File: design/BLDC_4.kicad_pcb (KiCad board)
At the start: 2 copper layers, 80 x 48.9 mm, 99 parts, among them J1 Conn_01x04, P1 PWR_COMM, P2 IN+, P3 IN-, P4 MOTOR3, P5 MOTOR2, P6 MOTOR1, P7 SWD, Q1 Si2302CDS, Q2 Si2302CDS, Q3 Si2302CDS, Q4 Si2302CDS, Q5 Si2302CDS, Q6 Si2302CDS, U1 DRV8302, U2 TC2117, U3 STM32F40X_LQFP64, X1 8MHz 10ppm

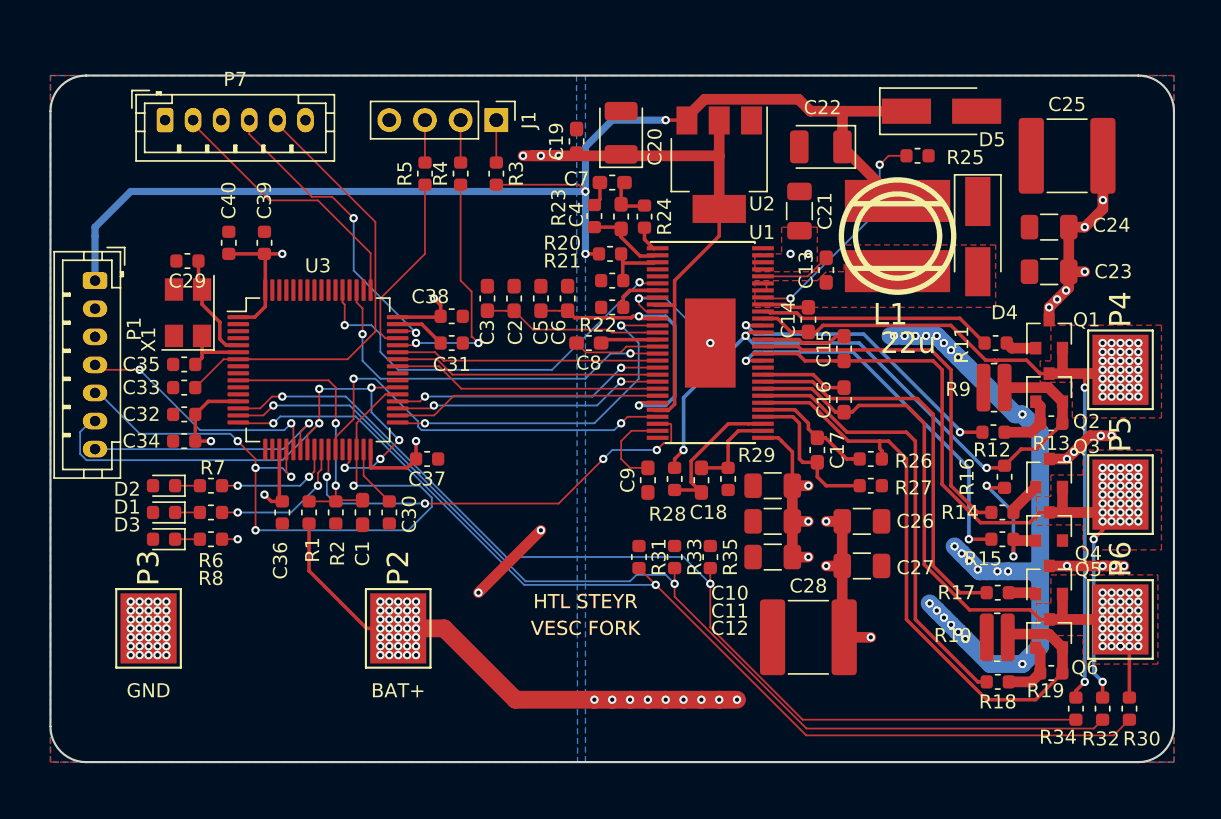
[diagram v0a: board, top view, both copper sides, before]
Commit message: Strengthening fills for output stage. Adding GND Fill
More to come :godmode:
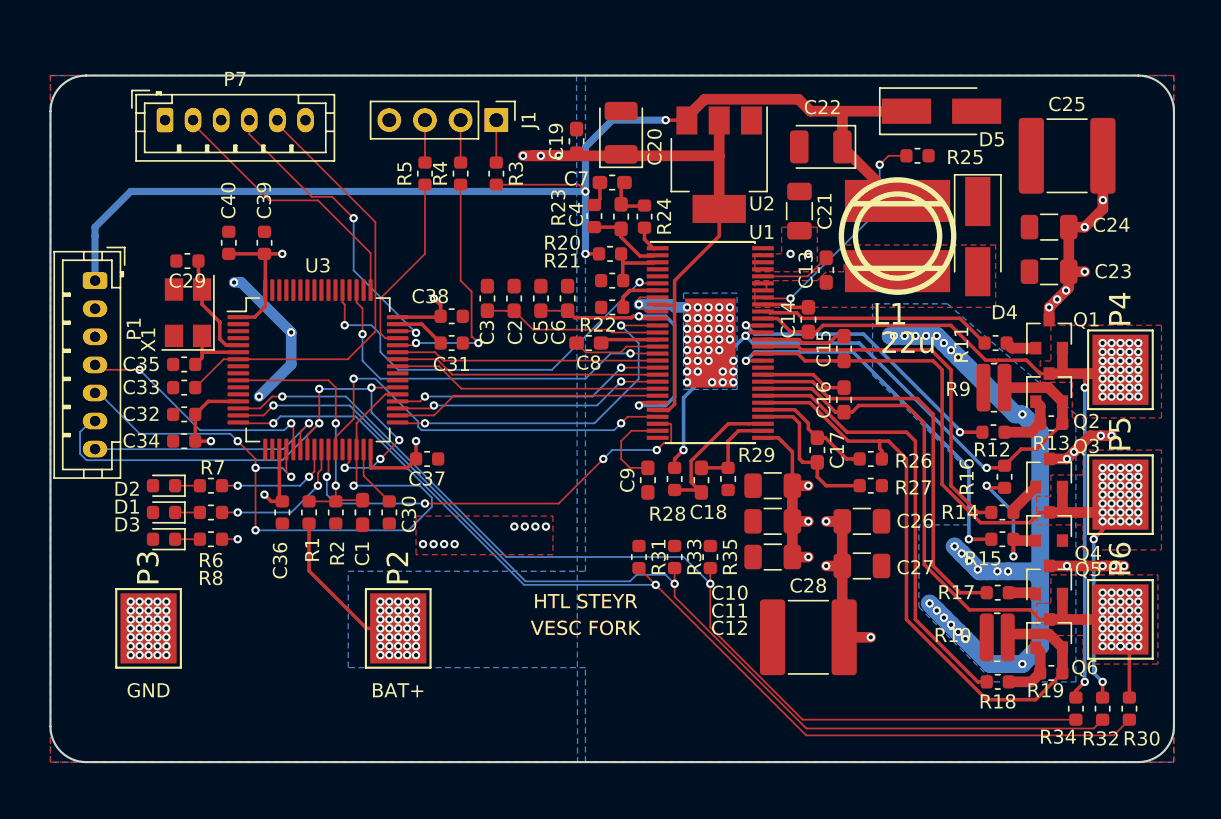
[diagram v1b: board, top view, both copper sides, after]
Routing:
- net V_SUPPLY: track 94.2 -> 68.0 mm, vias 66 -> 57
- net GND: track 59.1 -> 67.3 mm, vias 59 -> 97
- net VCC: track 80.1 -> 73.8 mm, vias 11 -> 17
- added copper zone on B.Cu, net GND
- added copper zone on F.Cu, net VCC

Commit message: Rework Board to fatten up supply
:snake: sneaky stuff :snake:
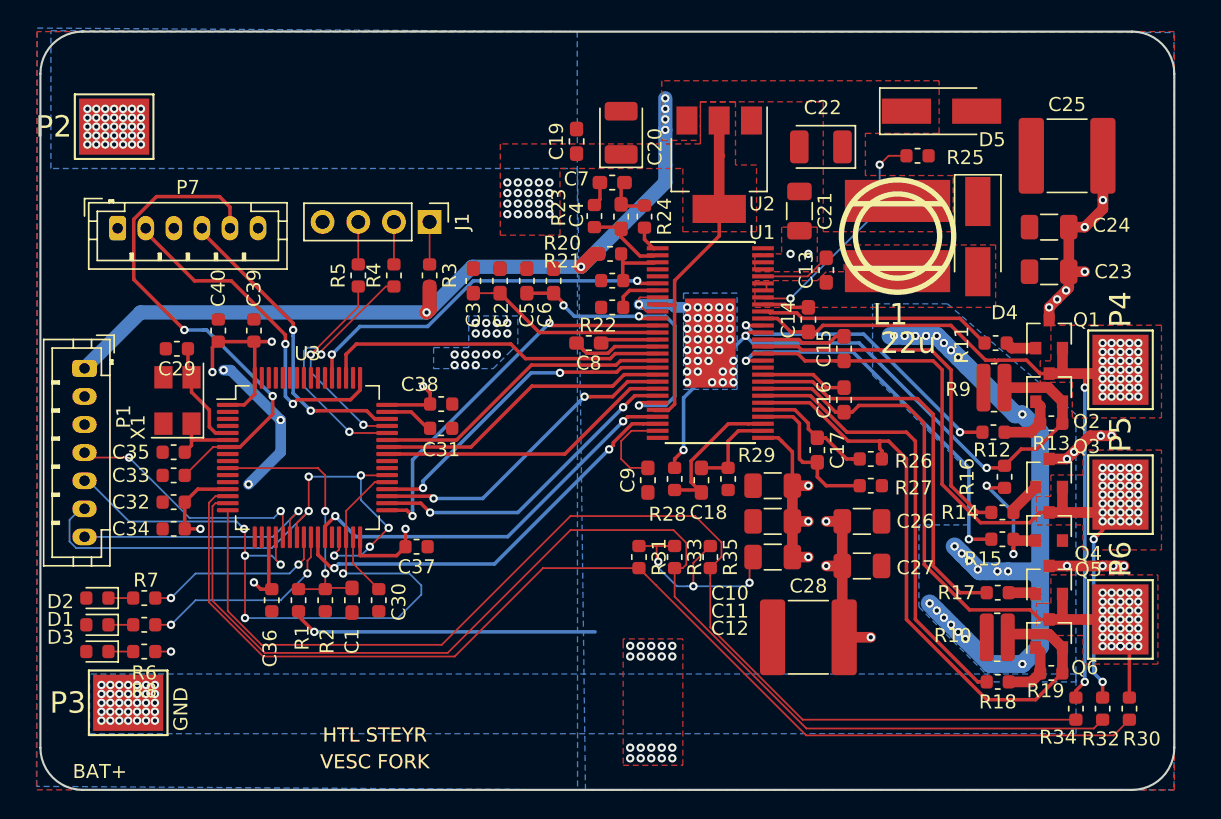
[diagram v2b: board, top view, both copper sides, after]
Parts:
- R10, R9: value 1mOhm -> 25mOhm
- moved P2 41.1 mm to (137.2, 59.5), turned to 90 degrees
- moved D1 9.30 mm to (136.1, 95.0)
- moved D2 9.30 mm to (136.1, 93.1)
- moved D3 9.30 mm to (136.1, 96.9)
- moved R6 9.30 mm to (139.4, 95.0)
- moved R7 9.30 mm to (139.4, 93.1)
- moved R8 9.30 mm to (139.4, 96.9)
- moved J1 8.67 mm to (159.7, 66.3)
- moved R3 8.67 mm to (159.7, 70.1)
- moved R4 8.67 mm to (157.2, 70.1)
- moved R5 8.67 mm to (154.6, 70.1)
- moved P7 8.40 mm to (137.5, 66.8)
- moved C1 6.29 mm to (154.2, 93.2)
- moved C29 6.29 mm to (141.7, 75.3)
- moved C30 6.29 mm to (156.1, 93.2)
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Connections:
- U3 pad 14: /MCU/SENS3 -> /MCU/SENS1
- U3 pad 16: /MCU/SENS1 -> /MCU/SENS3
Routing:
- net +5V: track 88.3 -> 56.7 mm, vias 3 -> 6
- net GND: track 67.3 -> 83.8 mm, vias 97 -> 116
- net VCC: track 73.8 -> 60.2 mm, vias 17 -> 27
- net /MCU/SENS2: track 73.7 -> 86.3 mm, vias 2 -> 0
- net /MCU/SENS3: track 72.5 -> 83.0 mm, vias 2 -> 0
- net V_SUPPLY: track 68.0 -> 78.5 mm, vias 57 -> 78
- net /MCU/SENS1: track 75.2 -> 83.8 mm, vias 2 -> 0
- net SWCLK: track 19.4 -> 24.5 mm, vias 0 -> 2
- net /MCU/LED_RED: track 10.3 -> 15.0 mm
- net /MCU/LED_GREEN: track 8.56 -> 13.3 mm
- net /MCU/L3: track 19.1 -> 23.0 mm, vias 0 -> 2
- net NRST: track 32.4 -> 36.3 mm, vias 0 -> 2
- net /MCU/L1: track 19.5 -> 23.1 mm
- net /MCU/L2: track 19.3 -> 22.8 mm
- net /MCU/H1: track 18.8 -> 21.6 mm
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- added copper zone on F.Cu, net +5V
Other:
- board size 80 x 48.9 mm -> 80.8 x 54 mm

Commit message: Infill change
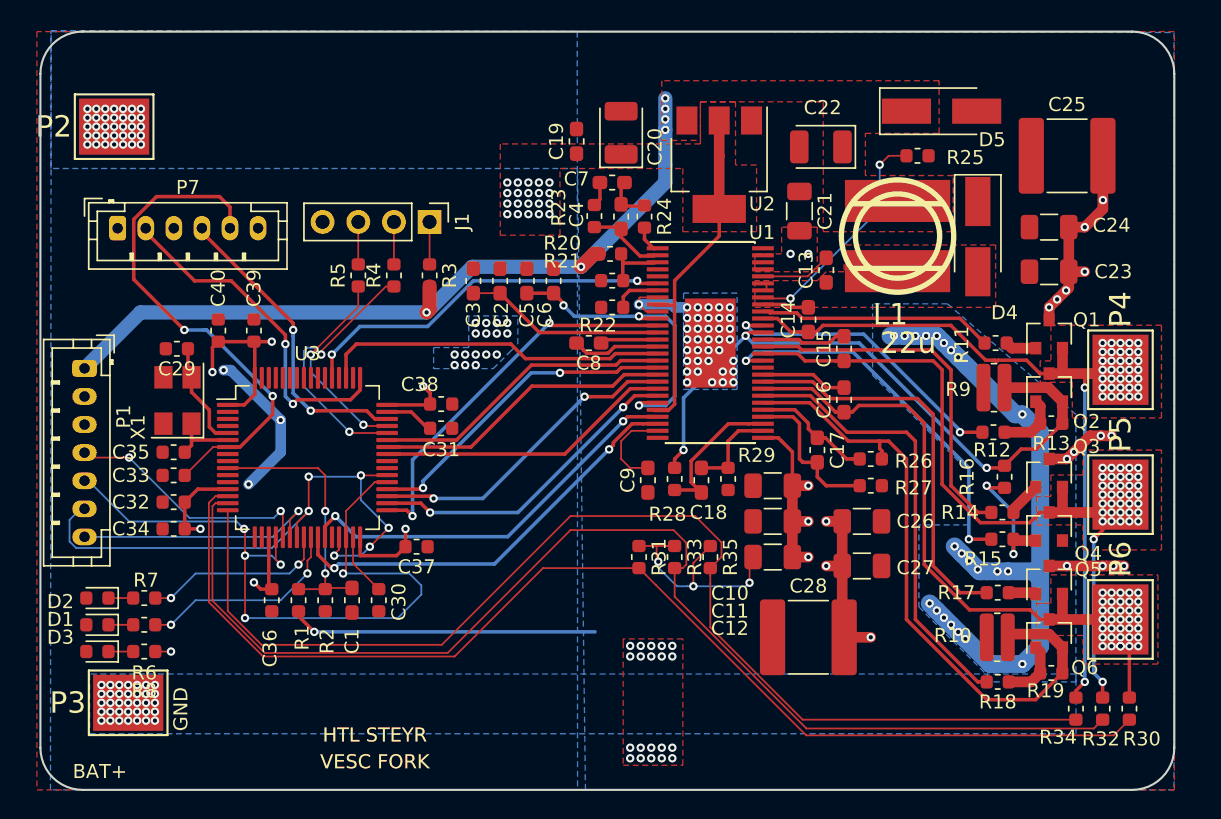
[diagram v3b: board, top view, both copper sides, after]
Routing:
- net GND: track 83.8 -> 37.9 mm, vias 116 -> 94
- net Net-(Q4-Pad1): track 9.67 -> 55.7 mm, vias 2 -> 24

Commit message: Fixed Crystal connection and footprint
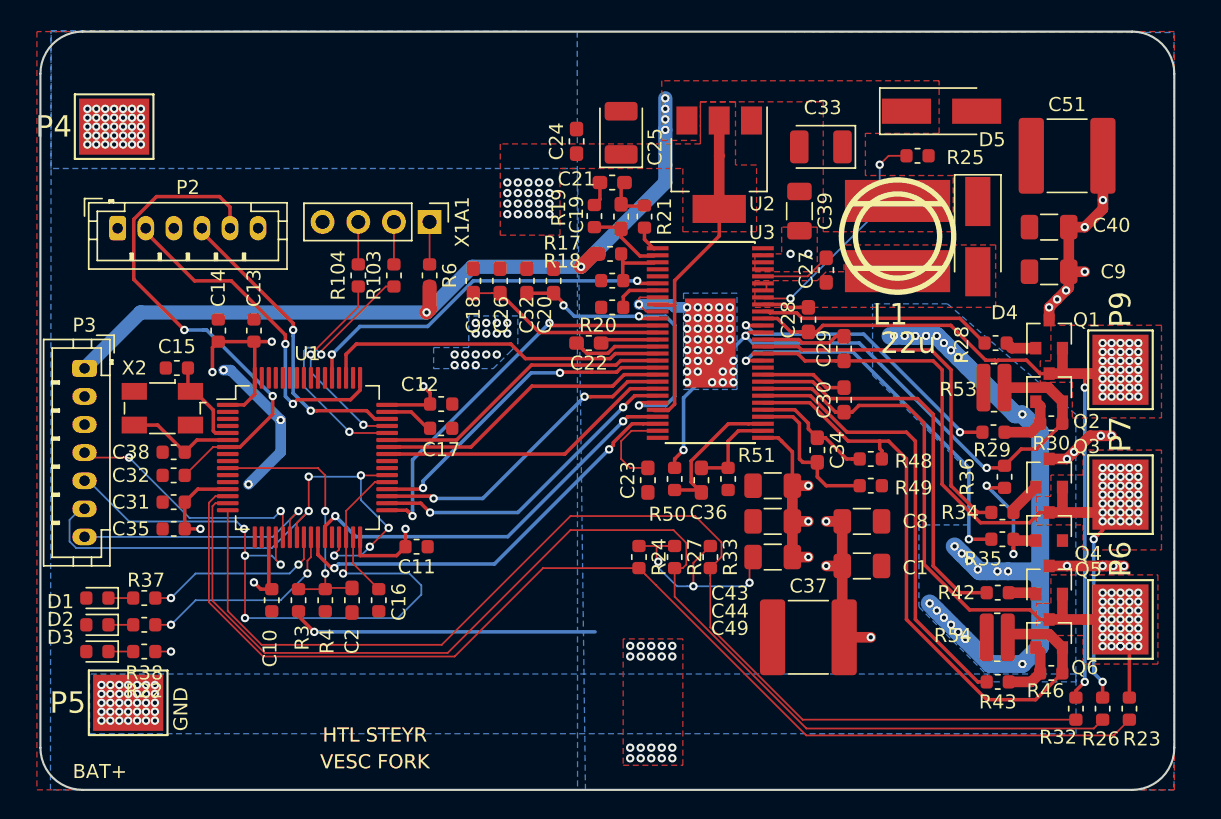
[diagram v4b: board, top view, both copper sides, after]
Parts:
- removed X1: 8MHz 10ppm, Crystal:Crystal_SMD_5032-4Pin_5.0x3.2mm
- added X2: 8MHz, Crystal:Crystal_SMD_Abracon_ABM3B-4Pin_5.0x3.2mm, F.Cu at (140.7, 79.6)
- moved C15 1.37 mm to (141.7, 76.7)
- renumbered C27 to C1, C36 to C10, C37 to C11, C38 to C12, C39 to C13, C40 to C14, C29 to C15, C30 to C16, C31 to C17, C3 to C18, C4 to C19, C1 to C2, C6 to C20, C7 to C21, C8 to C22, C9 to C23, C19 to C24, C20 to C25, C2 to C26, C13 to C27, C14 to C28, C15 to C29, C16 to C30, C32 to C31, C33 to C32, C22 to C33, C17 to C34, C34 to C35, C18 to C36, C28 to C37, C35 to C38, C21 to C39, C24 to C40, C10 to C43, C11 to C44, C12 to C49, C25 to C51, C5 to C52, C26 to C8, C23 to C9, D2 to D1, D1 to D2, P7 to P2, P1 to P3, P2 to P4, P3 to P5, P5 to P7, P4 to P9, R4 to R103, R5 to R104, R20 to R17, R21 to R18, R23 to R19, R22 to R20, R24 to R21, R8 to R22, R30 to R23, R31 to R24, R32 to R26, R33 to R27, R11 to R28, R12 to R29, R1 to R3, R13 to R30, R34 to R32, R35 to R33, R14 to R34, R15 to R35, R16 to R36, R7 to R37, R6 to R38, R2 to R4, R17 to R42, R18 to R43, R19 to R46, R26 to R48, R27 to R49, R28 to R50, R29 to R51, R9 to R53, R10 to R54, R3 to R6, U3 to U1, U1 to U3, J1 to X1A1
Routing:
- net Net-(C38-Pad1): track 4.81 -> 7.82 mm
- net Net-(C15-Pad1): track 7.68 -> 6.49 mm

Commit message: v0.2 Bug fixes and improvements
Fixed wrong GND net near shunts
Seperated GND and PWRGND
Added another GND net for capacitors near output stage
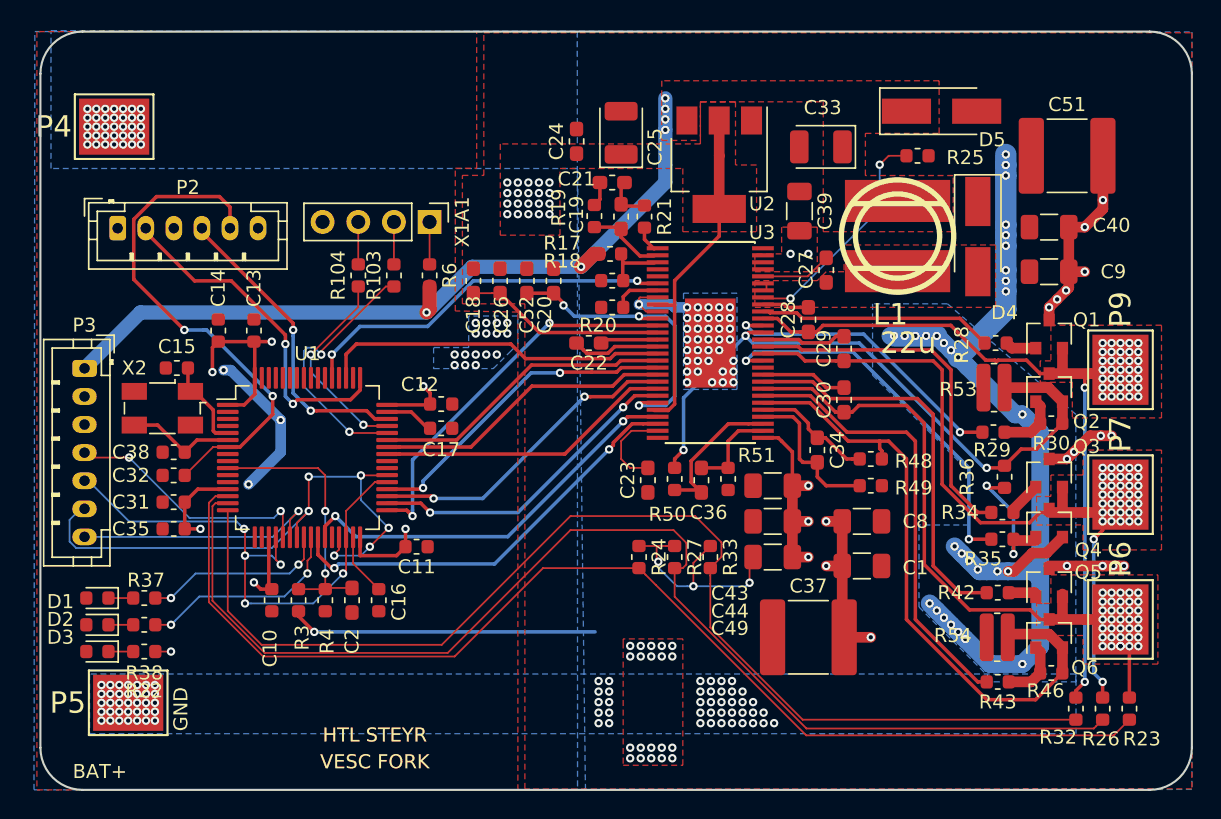
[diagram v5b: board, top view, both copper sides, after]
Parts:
- moved Q4 0.25 mm to (203.8, 87.8)
- moved Q5 0.19 mm to (203.8, 92.0)
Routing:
- net GND: track 37.9 -> 107.6 mm, vias 94 -> 165
- net Net-(Q4-Pad1): track 55.7 -> 9.67 mm, vias 24 -> 2
- net /TX_SDA: track 52.2 -> 39.2 mm
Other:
- board size 80.8 x 54 mm -> 82 x 54 mm
